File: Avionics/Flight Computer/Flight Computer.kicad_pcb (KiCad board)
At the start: 4 copper layers, 50 x 40 mm, 198 parts, among them J1 ERF8-040-05.0-S-DV-K, J2 ERF8-040-05.0-S-DV-K, J3 473460001, J4 734120110, J5 734120110, J6 734120110, U1 CC1310F128RGZR, U10 Logo, U11 Logo, U12 ATSAME70Q21A-AN, U2 CC1190RGVR, U3 CC2650F128RGZR, U4 CC2592RGVR, U5 MPU-9250, U6 LP5521YQ, U7 LPS25HB, U8 MAX17243, U9 MAX-M8W, Y1 9HT11-32.768KDZB-T, Y2 7V-16.000MAHJ-T, Y3 XRCGB24M000F2P00R0, Y5 XRCGB24M000F2P00R0

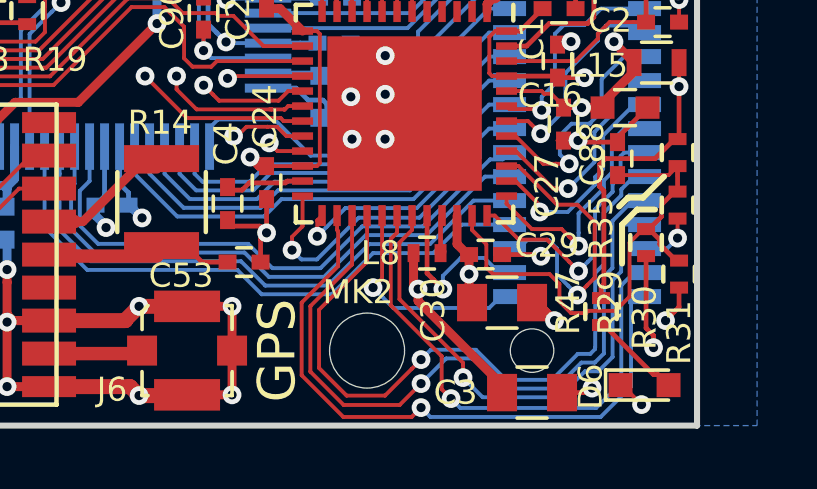
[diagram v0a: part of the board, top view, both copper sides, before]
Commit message: Built outputs and added manufacturing part numbers to make BOM search easier.
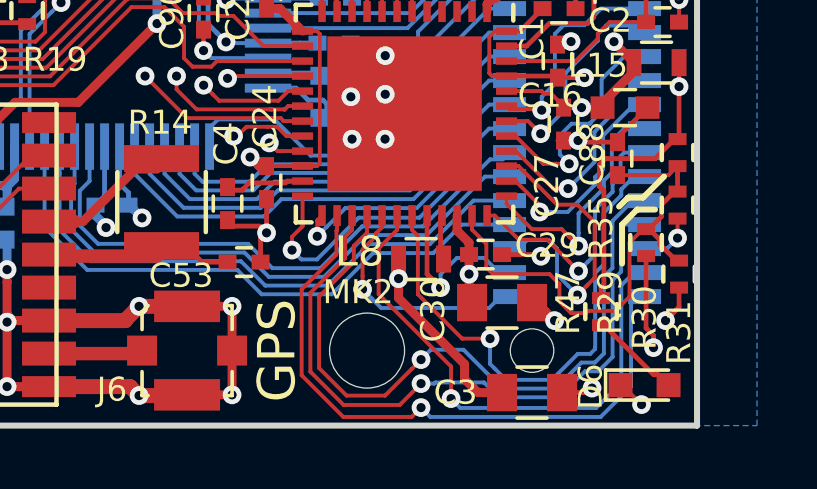
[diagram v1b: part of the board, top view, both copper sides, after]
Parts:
- C1, C2: value 0.1 -> 0.1u
- C10, C8: value 2.2p -> CL05C2R2BB5NNNC
- C12: value 18p -> CL05C2R2BB5NNNC
- C13, C21, C9: value 47p -> GRM1555C1H470FA01D
- C15, C17, C18, C26, C60, C62, C63, C64, C65, C66, C67, C70, C71: value 12p -> GRM1555C1H120GA01D
- C16, C38, C39, C46: value 2.2u -> EMK107BJ225KA-T
- C19, C3, C30, C33, C44, C51, C52: value 22u -> EMK212BBJ226MG-T
- C48, C49: value 10u -> GRM31CR61H106MA12L
- C50: value 2.2u -> UMK212BB7225KG-T
- L1, L14: value 22n -> CIH10T22NJNC
- L13, L3: value 2.2n -> HK10052N2S-T
- L4: value 9.1n -> LQW18AN9N1D00D
- L5: value 4.7n -> HK10054N7S-T
- L6: value 1n -> LQG15HS1N0S02D
- L7: value 2n -> LQG15HS2N0S02D
- L8: value 6.8u -> BRL1608T6R8M; footprint Inductors_SMD:L_0402 -> Inductors_SMD:L_0603
- L9: value 10u -> MLZ1608N100LT000
- R14: value 10 -> ERJ-14YJ100U
- R21: value 22k -> 18k
- U8: value MAX17243 -> MAX17243ETPB
- U9: value MAX-M8W -> MAX-M8W-0
- moved L8 0.28 mm to (90.8, 119.5)
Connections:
- J2 pad 69: /Connectors/900-DIO-18 -> /Connectors/900-DIO-21
- J2 pad 71: /Connectors/900-DIO-17 -> /Connectors/900-DIO-18
- J2 pad 73: /Connectors/900-DIO-21 -> /Connectors/900-DIO-17
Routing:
- net /900MHz Radio/VDDR_CC1310: track 24.6 -> 25.9 mm
- net /Connectors/900-DIO-17: track 23.9 -> 22.6 mm
- net /Connectors/900-DIO-19: track 7.51 -> 8.04 mm

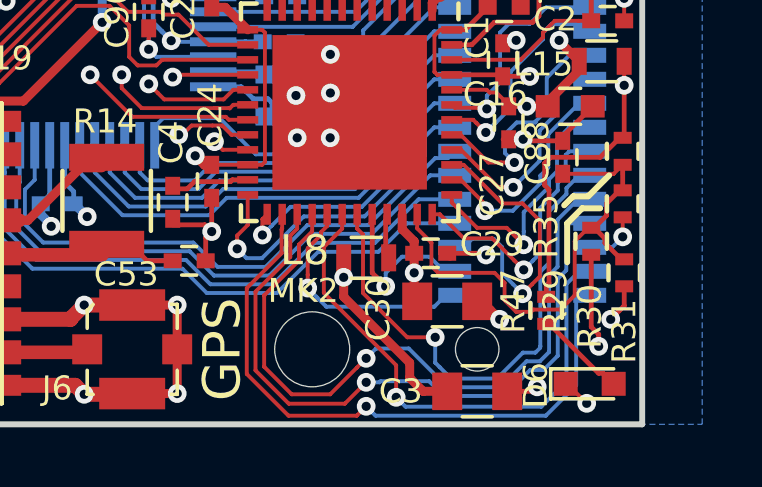
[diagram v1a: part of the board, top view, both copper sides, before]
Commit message: Rebuilt output files and generated a few BOM fixes.
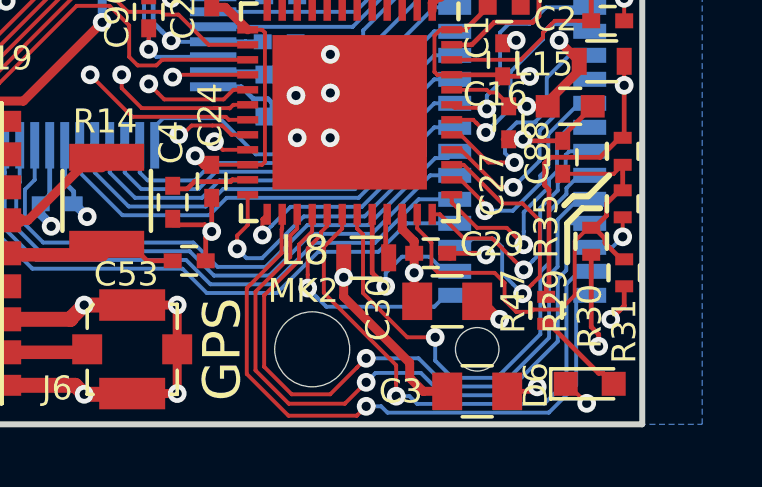
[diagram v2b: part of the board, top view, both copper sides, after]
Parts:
- C11: value 0.2p -> DNP
- C14: value 1p -> CL05C2R2BB5NNNC
- C5: value 3.3p -> GJM1555C1H3R3CB01D
- C6: value 7.5p -> GJM1555C1H7R5CB01D
- C85, C86: value 4.7u -> CC0603KRX5R7BB475
- L12, L18: value 10n -> LQG15HN9N1J02D
- L2: value 7.5n -> LQG15HS7N5J02D
- L4: value LQW18AN9N1D00D -> LQG15HN9N1J02D
- R20: value 5.62k -> 5.6k
- R23: value 2.2 -> ERJ-2GEJ2R2X
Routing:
- net /Connectors/900-DIO-18: track 23.6 -> 23.0 mm

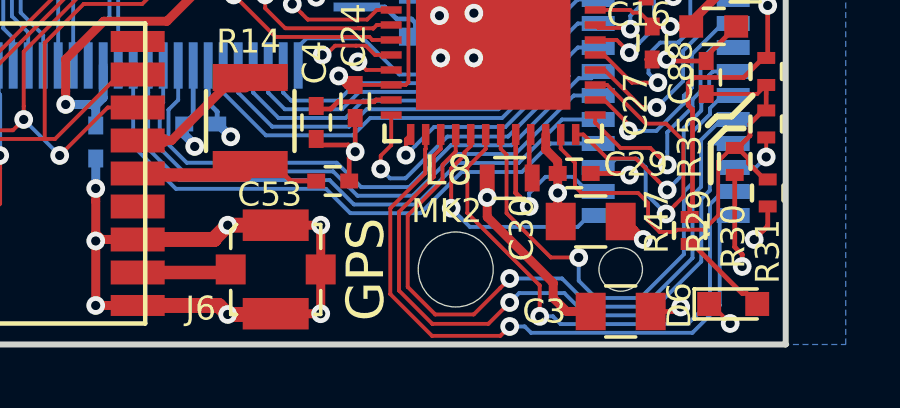
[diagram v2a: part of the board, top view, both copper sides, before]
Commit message: Updated more manufacturing part numbers for macrofab compatibility.
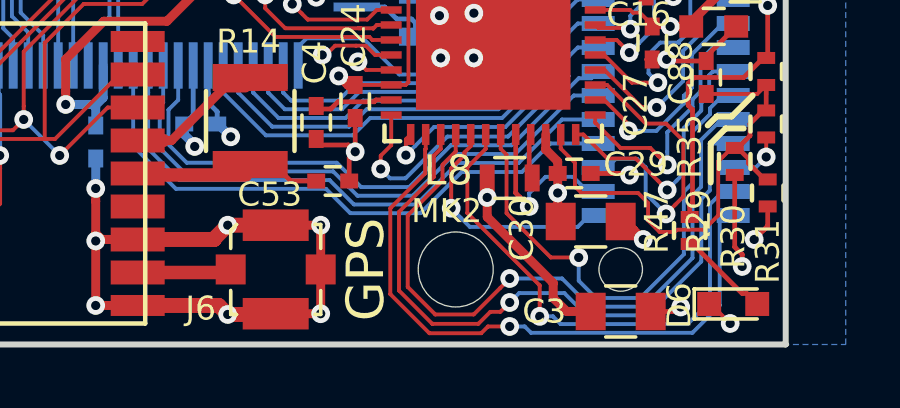
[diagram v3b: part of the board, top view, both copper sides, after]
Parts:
- C92, C93: value 0.47u -> GRM155R61C474KE01D
- D3: value CLX6D-FKB -> CLX6D-FKB-CMPQSGKBB7A363
- D4, D5, D8: value LED-0603-GREEN -> MF-LED-0603-GREEN
- D6: value LED-0603-RED -> MF-LED-0603-RED
- J4, J5, J6: value 734120110 -> 0734120110
- L10, L11, L15: value BLM18HE152SN1 -> BLM18HE152SN1D
- R4: value 3.3k -> RC0402FR-073K3L
- R8: value 3.9k -> RC0402FR-073K9L
- U6: value LP5521YQ -> LP5521YQ/NOPB
- U7: value LPS25HB -> LPS25HBTR
- U8: value MAX17243ETPB -> MAX17243ETPB+

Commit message: Fixed connector part number
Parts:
- J1, J2: value ERF8-040-05.0-S-DV-K -> ERF8-040-05.0-S-DV-K-TR
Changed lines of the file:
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@@
       (effects (font (size 0.8 0.8) (thickness 0.13)) (justify mirror))
     )
-    (fp_text value ERF8-040-05.0-S-DV-K (at 0 0 90) (layer B.Fab)
+    (fp_text value ERF8-040-05.0-S-DV-K-TR (at 0 0 90) (layer B.Fab)
       (effects (font (size 0.9 0.9) (thickness 0.1)) (justify mirror))
     )
@@
       (effects (font (size 0.8 0.8) (thickness 0.13)) (justify mirror))
     )
-    (fp_text value ERF8-040-05.0-S-DV-K (at 0 0 90) (layer B.Fab)
+    (fp_text value ERF8-040-05.0-S-DV-K-TR (at 0 0 90) (layer B.Fab)
       (effects (font (size 0.9 0.9) (thickness 0.1)) (justify mirror))
     )

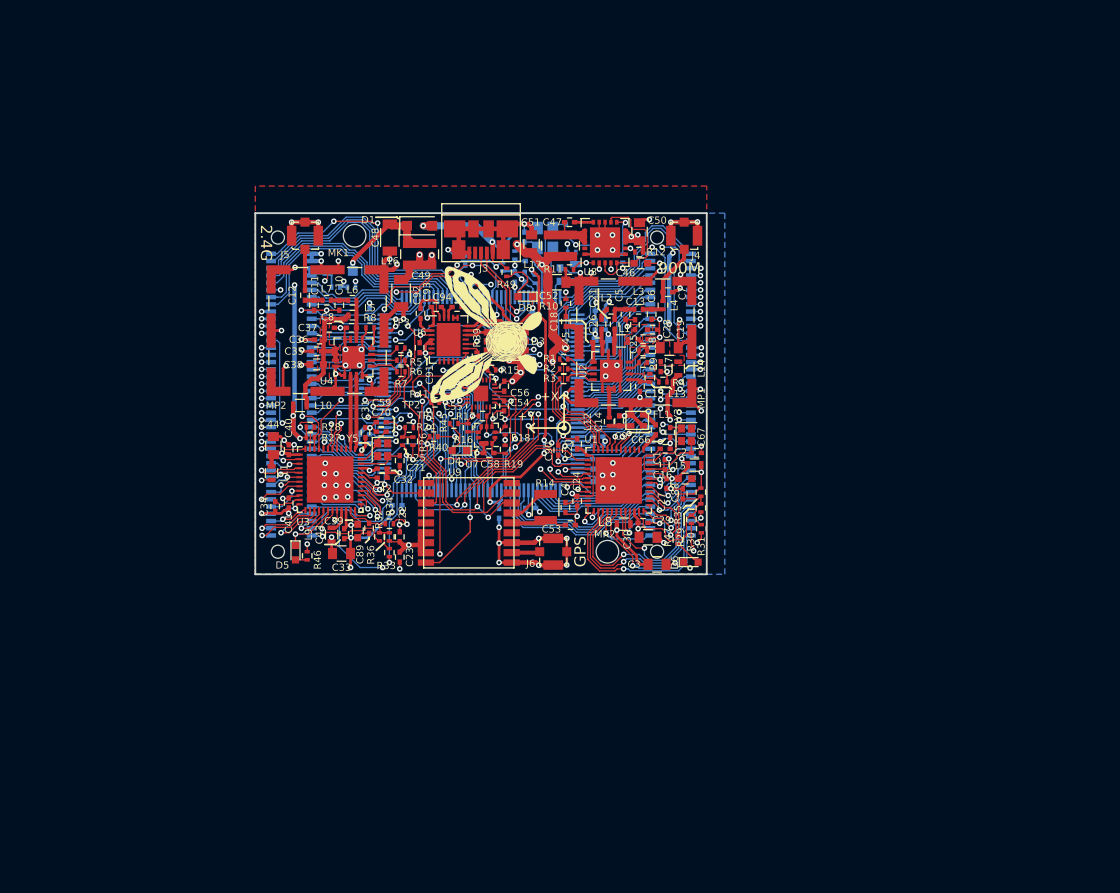
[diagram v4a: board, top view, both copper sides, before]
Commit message: Finished rerouting and power supply update. Replaced connectors and did initial replacement.
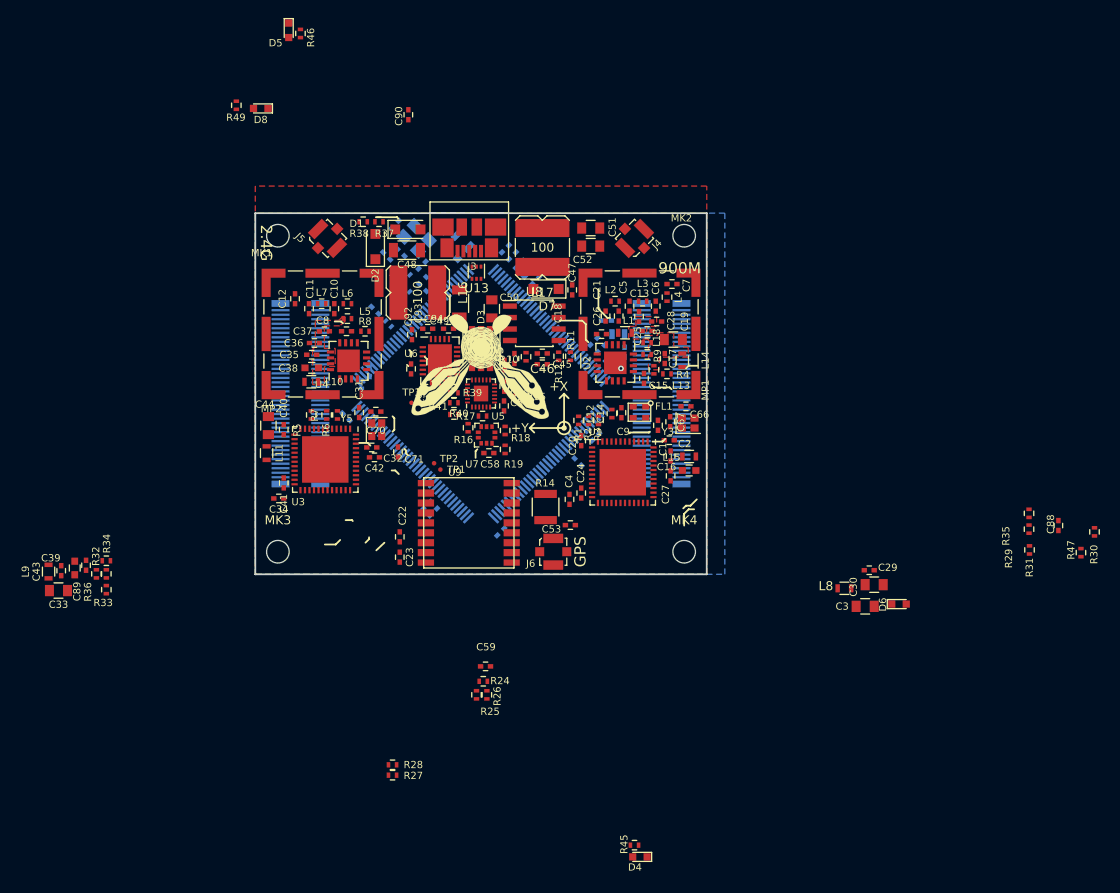
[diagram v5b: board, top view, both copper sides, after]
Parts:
- removed R13: 10k, Resistors_SMD:R_0402
- added C95: GRM1555C1H120GA01D, Capacitors_SMD:C_0402, F.Cu at (78.7, 101.1)
- added D7: SS24FL, Diodes_SMD:D_SOD-123F, F.Cu at (82.2, 93.4)
- added MK3: Mounting_Hole, Mounting_Holes:MountingHole_2.5mm, F.Cu at (52.5, 122.5)
- added MK4: Mounting_Hole, Mounting_Holes:MountingHole_2.5mm, F.Cu at (97.5, 122.5)
- added U13: NUF2042XV6, TO_SOT_Packages_SMD:SOT-563, F.Cu at (74.5, 91.6)
- C45: value 1n -> 0.01u
- C46: value EMK107BJ225KA-T -> GRM1555C1H120GA01D; footprint Capacitors_SMD:C_0603 -> Capacitors_SMD:C_0402
- D1: value NTS245SFT1G -> SS24FL
- D2: value NTS245SFT1G -> SS24FL; moved to F.Cu
- J1, J2: value ERF8-040-05.0-S-DV-K-TR -> AXK5S80047YG; footprint Connectors_Samtec:ERF8-040-05.0-S-DV-K -> Connectors:AXK5S80047YG
- L16, L17: value 74438356022 -> SRN6045-100M; footprint Inductors_SMD:L_Wuerth_MAPI-4020 -> Inductors_SMD:L_BOURNS-SRN6045
- R11: value 15k -> 18k
- R12: value 100k -> ERJ-2RKF5761X
- R37, R38: moved to F.Cu
- U8: value MAX17243ETPB+ -> TPS54232; footprint Housings_DFN_QFN:QFN-20-1EP_5x5mm_Pitch0.65mm -> Housings_SOIC:SOIC-8_3.9x4.9mm_Pitch1.27mm
- moved R46 57.9 mm to (55.0, 65.1)
- moved D5 57.9 mm to (53.7, 64.8)
- moved R45 50.8 mm to (92.0, 155.0)
- moved D4 49.2 mm to (92.6, 156.3)
- moved R30 44.7 mm to (143.0, 120.3)
- moved R47 44.7 mm to (141.4, 122.6)
- moved C88 41.7 mm to (138.9, 119.6)
- moved C90 40.7 mm to (67.0, 74.1)
- moved R28 38.5 mm to (65.2, 146.1)
- moved R27 38.5 mm to (65.2, 147.2)
- moved R31 36.4 mm to (135.8, 122.3)
- moved R29 36.4 mm to (135.7, 120.0)
- moved R35 36.4 mm to (135.7, 118.2)
- moved MK2 36.0 mm to (97.5, 87.5)
- moved D8 36.0 mm to (50.6, 73.4)
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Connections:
- C46 pad 1: /Power/BIAS -> GND
- C46 pad 2: GND -> Net-(C46-Pad2)
- J1 pad 1: GND -> Net-(J1-Pad1)
- J1 pad 10: /Connectors/PA31 -> Net-(J1-Pad10)
- J1 pad 11: /Connectors/PD9 -> Net-(J1-Pad11)
- J1 pad 12: /Connectors/PA29 -> Net-(J1-Pad12)
- J1 pad 13: /Connectors/PC18 -> Net-(J1-Pad13)
- J1 pad 14: /Connectors/PC19 -> Net-(J1-Pad14)
- J1 pad 15: /Connectors/PA28 -> Net-(J1-Pad15)
- J1 pad 16: /Connectors/PA30 -> Net-(J1-Pad16)
- J1 pad 17: /Connectors/PD8 -> Net-(J1-Pad17)
- J1 pad 18: +3V3 -> Net-(J1-Pad18)
- J1 pad 19: /Connectors/PD15 -> Net-(J1-Pad19)
- J1 pad 2: /Connectors/PC21 -> Net-(J1-Pad2)
- J1 pad 20: +3V3 -> Net-(J1-Pad20)
- J1 pad 21: /Connectors/PB4 -> Net-(J1-Pad21)
- J1 pad 22: GND -> Net-(J1-Pad22)
- J1 pad 23: /Connectors/PC17 -> Net-(J1-Pad23)
- J1 pad 24: GND -> Net-(J1-Pad24)
- J1 pad 25: /Connectors/PA0 -> Net-(J1-Pad25)
- J1 pad 26: /Connectors/PB12 -> Net-(J1-Pad26)
- J1 pad 27: /Connectors/PD10 -> Net-(J1-Pad27)
- J1 pad 28: /Connectors/PD25 -> Net-(J1-Pad28)
- J1 pad 29: /Connectors/PC16 -> Net-(J1-Pad29)
- J1 pad 3: GND -> Net-(J1-Pad3)
- J1 pad 30: /Connectors/PD26 -> Net-(J1-Pad30)
- J1 pad 31: /Connectors/PA1 -> Net-(J1-Pad31)
- J1 pad 32: /Connectors/PC6 -> Net-(J1-Pad32)
- J1 pad 33: /Connectors/PD11 -> Net-(J1-Pad33)
- J1 pad 34: /Connectors/PD24 -> Net-(J1-Pad34)
- J1 pad 35: /Connectors/PC14 -> Net-(J1-Pad35)
- J1 pad 36: /Connectors/PA24 -> Net-(J1-Pad36)
- J1 pad 37: /Connectors/PC11 -> Net-(J1-Pad37)
- J1 pad 38: /Connectors/PC5 -> Net-(J1-Pad38)
- J1 pad 39: /CPU-SDA -> Net-(J1-Pad39)
- J1 pad 4: /Connectors/PD6 -> Net-(J1-Pad4)
- J1 pad 40: /Connectors/PA25 -> Net-(J1-Pad40)
- J1 pad 41: /Connectors/PC10 -> Net-(J1-Pad41)
- J1 pad 42: /Connectors/PA26 -> Net-(J1-Pad42)
- J1 pad 43: /Connectors/PB7 -> Net-(J1-Pad43)
- J1 pad 44: /Connectors/PA11 -> Net-(J1-Pad44)
- J1 pad 45: /Connectors/PC9 -> Net-(J1-Pad45)
- J1 pad 46: /Connectors/PA12 -> Net-(J1-Pad46)
- J1 pad 47: /Connectors/PC8 -> Net-(J1-Pad47)
- J1 pad 48: /Connectors/PA27 -> Net-(J1-Pad48)
- J1 pad 49: /Connectors/PD16 -> Net-(J1-Pad49)
- J1 pad 5: +BATT -> Net-(J1-Pad5)
- J1 pad 50: /Connectors/PD28 -> Net-(J1-Pad50)
- J1 pad 51: /CPU-SCK -> Net-(J1-Pad51)
- J1 pad 52: /CPU_RESET_EXT -> Net-(J1-Pad52)
- J1 pad 53: /Connectors/PC28 -> Net-(J1-Pad53)
- J1 pad 54: /Connectors/PB6 -> Net-(J1-Pad54)
- J1 pad 55: /Connectors/PD17 -> Net-(J1-Pad55)
- J1 pad 56: /Connectors/2.4-DIO-7 -> Net-(J1-Pad56)
- J1 pad 57: /Connectors/2.4-ADIO-30 -> Net-(J1-Pad57)
- J1 pad 58: /Connectors/2.4-DIO-8 -> Net-(J1-Pad58)
- J1 pad 59: /Connectors/2.4-ADIO-29 -> Net-(J1-Pad59)
- J1 pad 6: /Connectors/PC20 -> Net-(J1-Pad6)
- J1 pad 60: /Connectors/2.4-DIO-9 -> Net-(J1-Pad60)
- J1 pad 61: /Connectors/2.4-ADIO-28 -> Net-(J1-Pad61)
- J1 pad 62: /Connectors/2.4-DIO-10 -> Net-(J1-Pad62)
- J1 pad 63: /Connectors/2.4-ADIO-27 -> Net-(J1-Pad63)
- J1 pad 64: /Connectors/2.4-DIO-11 -> Net-(J1-Pad64)
- J1 pad 65: /Connectors/2.4-ADIO-26 -> Net-(J1-Pad65)
- J1 pad 66: /Connectors/2.4-DIO-12 -> Net-(J1-Pad66)
- J1 pad 67: /Connectors/2.4-ADIO-25 -> Net-(J1-Pad67)
- J1 pad 68: /Connectors/2.4-DIO-13 -> Net-(J1-Pad68)
- J1 pad 69: /Connectors/2.4-ADIO-24 -> Net-(J1-Pad69)
- J1 pad 7: +BATT -> Net-(J1-Pad7)
- J1 pad 70: /Connectors/2.4-DIO-14 -> Net-(J1-Pad70)
- J1 pad 71: /Connectors/2.4-ADIO-23 -> Net-(J1-Pad71)
- J1 pad 72: /Connectors/2.4-DIO-15 -> Net-(J1-Pad72)
- J1 pad 73: /Connectors/2.4-DIO-18 -> Net-(J1-Pad73)
- J1 pad 74: /2.4-TMSC -> Net-(J1-Pad74)
- J1 pad 75: /Connectors/2.4-DIO-19 -> Net-(J1-Pad75)
- J1 pad 76: /2.4-TCKC -> Net-(J1-Pad76)
- J1 pad 77: /Connectors/2.4-DIO-20 -> Net-(J1-Pad77)
- J1 pad 78: /Connectors/2.4-DIO-16 -> Net-(J1-Pad78)
- J1 pad 79: /2.4_RESET_EXT -> Net-(J1-Pad79)
- J1 pad 8: /Connectors/PD7 -> Net-(J1-Pad8)
- J1 pad 80: /Connectors/2.4-DIO-17 -> Net-(J1-Pad80)
- J1 pad 9: /Connectors/PB5 -> Net-(J1-Pad9)
- J2 pad 1: /Connectors/PB13 -> Net-(J2-Pad1)
- J2 pad 10: /Connectors/PD31 -> Net-(J2-Pad10)
- J2 pad 11: /Connectors/PC25 -> Net-(J2-Pad11)
- J2 pad 12: /Connectors/PE0 -> Net-(J2-Pad12)
- J2 pad 13: /Connectors/PD1 -> Net-(J2-Pad13)
- J2 pad 14: /Connectors/PC27 -> Net-(J2-Pad14)
- J2 pad 15: /Connectors/PD2 -> Net-(J2-Pad15)
- J2 pad 16: /Connectors/PC26 -> Net-(J2-Pad16)
- J2 pad 17: /Connectors/PD3 -> Net-(J2-Pad17)
- J2 pad 18: /Connectors/PC31 -> Net-(J2-Pad18)
- J2 pad 19: /Connectors/PD4 -> Net-(J2-Pad19)
- J2 pad 2: /Connectors/PE3 -> Net-(J2-Pad2)
- J2 pad 20: /Connectors/PC30 -> Net-(J2-Pad20)
- J2 pad 21: /Connectors/PD5 -> Net-(J2-Pad21)
- J2 pad 22: /Connectors/PC29 -> Net-(J2-Pad22)
- J2 pad 23: /Power-Good -> Net-(J2-Pad23)
- J2 pad 24: /Connectors/PC12 -> Net-(J2-Pad24)
- J2 pad 25: /Power-~SHDN~ -> Net-(J2-Pad25)
- J2 pad 26: /Connectors/PC15 -> Net-(J2-Pad26)
- J2 pad 27: +3V3 -> Net-(J2-Pad27)
- J2 pad 28: /Connectors/PC13 -> Net-(J2-Pad28)
- J2 pad 29: +3V3 -> Net-(J2-Pad29)
- J2 pad 3: /Connectors/PC0 -> Net-(J2-Pad3)
- J2 pad 30: /Connectors/PB1 -> Net-(J2-Pad30)
- J2 pad 31: GND -> Net-(J2-Pad31)
- J2 pad 32: /Connectors/PB0 -> Net-(J2-Pad32)
- J2 pad 33: GND -> Net-(J2-Pad33)
- J2 pad 34: /Connectors/PA20 -> Net-(J2-Pad34)
- J2 pad 35: /Connectors/PA14 -> Net-(J2-Pad35)
- J2 pad 36: /Connectors/PA19 -> Net-(J2-Pad36)
- J2 pad 37: /Connectors/PA15 -> Net-(J2-Pad37)
- J2 pad 38: /Connectors/PA18 -> Net-(J2-Pad38)
- J2 pad 39: /Connectors/AUX_SCL -> Net-(J2-Pad39)
- J2 pad 4: /Connectors/PE2 -> Net-(J2-Pad4)
- J2 pad 40: /Connectors/PA17 -> Net-(J2-Pad40)
- J2 pad 41: /Connectors/AUX_SDA -> Net-(J2-Pad41)
- J2 pad 42: /Connectors/PB2 -> Net-(J2-Pad42)
- J2 pad 43: /Connectors/900-DIO-10 -> Net-(J2-Pad43)
- J2 pad 44: /Connectors/PE4 -> Net-(J2-Pad44)
- J2 pad 45: /Connectors/900-DIO-11 -> Net-(J2-Pad45)
- J2 pad 46: /Connectors/PE5 -> Net-(J2-Pad46)
- J2 pad 47: /Connectors/900-DIO-12 -> Net-(J2-Pad47)
- J2 pad 48: /Connectors/PB3 -> Net-(J2-Pad48)
- J2 pad 49: /Connectors/900-DIO-13 -> Net-(J2-Pad49)
- J2 pad 5: /Connectors/PC22 -> Net-(J2-Pad5)
- J2 pad 50: /Connectors/PA21 -> Net-(J2-Pad50)
- J2 pad 51: /Connectors/900-DIO-14 -> Net-(J2-Pad51)
- J2 pad 52: /Connectors/PA22 -> Net-(J2-Pad52)
- J2 pad 53: /Connectors/900-DIO-15 -> Net-(J2-Pad53)
- J2 pad 54: /Connectors/PC1 -> Net-(J2-Pad54)
- J2 pad 55: /Connectors/900-ADIO-30 -> Net-(J2-Pad55)
- J2 pad 56: /Connectors/PC2 -> Net-(J2-Pad56)
- J2 pad 57: /Connectors/900-ADIO-29 -> Net-(J2-Pad57)
- J2 pad 58: /Connectors/PC3 -> Net-(J2-Pad58)
- J2 pad 59: /Connectors/900-ADIO-28 -> Net-(J2-Pad59)
- J2 pad 6: /Connectors/PE1 -> Net-(J2-Pad6)
- J2 pad 60: /Connectors/PC4 -> Net-(J2-Pad60)
- J2 pad 61: /Connectors/900-ADIO-27 -> Net-(J2-Pad61)
- J2 pad 62: /Connectors/PA13 -> Net-(J2-Pad62)
- J2 pad 63: /Connectors/900-ADIO-25 -> Net-(J2-Pad63)
- J2 pad 64: /900-TCKC -> Net-(J2-Pad64)
- J2 pad 65: /Connectors/900-ADIO-24 -> Net-(J2-Pad65)
- J2 pad 66: /900-TMSC -> Net-(J2-Pad66)
- J2 pad 67: /Connectors/900-ADIO-23 -> Net-(J2-Pad67)
- J2 pad 68: /Connectors/PA16 -> Net-(J2-Pad68)
- J2 pad 69: /Connectors/900-DIO-21 -> Net-(J2-Pad69)
- J2 pad 7: /Connectors/PC23 -> Net-(J2-Pad7)
- J2 pad 70: /Connectors/PA23 -> Net-(J2-Pad70)
- J2 pad 71: /Connectors/900-DIO-18 -> Net-(J2-Pad71)
- J2 pad 72: /Connectors/PD27 -> Net-(J2-Pad72)
- J2 pad 73: /Connectors/900-DIO-17 -> Net-(J2-Pad73)
- J2 pad 74: /Connectors/PC7 -> Net-(J2-Pad74)
- J2 pad 75: /900_RESET_EXT -> Net-(J2-Pad75)
- J2 pad 76: /Connectors/900-ADIO-26 -> Net-(J2-Pad76)
- J2 pad 77: /Connectors/900-DIO-20 -> Net-(J2-Pad77)
- J2 pad 78: /Connectors/900-DIO-22 -> Net-(J2-Pad78)
- J2 pad 79: /Connectors/900-DIO-16 -> Net-(J2-Pad79)
- J2 pad 8: /Connectors/PD0 -> Net-(J2-Pad8)
- J2 pad 80: /Connectors/900-DIO-19 -> Net-(J2-Pad80)
- J2 pad 9: /Connectors/PC24 -> Net-(J2-Pad9)
- J3 pad 2: /Connectors/USBD_N -> Net-(J3-Pad2)
- J3 pad 3: /Connectors/USBD_P -> Net-(J3-Pad3)
- R10 pad 1: Net-(R10-Pad1) -> Net-(C46-Pad2)
- R11 pad 1: Net-(R11-Pad1) -> +3V3
- R11 pad 2: GND -> Net-(R11-Pad2)
- R12 pad 1: Net-(C49-Pad1) -> Net-(R11-Pad2)
- R12 pad 2: /Power-~SHDN~ -> GND
- U8 pad 1: Net-(R11-Pad1) -> Net-(C47-Pad2)
- U8 pad 2: +3V3 -> Net-(C49-Pad1)
- U8 pad 3: /Power/BIAS -> /Power-~SHDN~
- U8 pad 4: Net-(R10-Pad1) -> Net-(C95-Pad2)
- U8 pad 5: /Power/BIAS -> Net-(R11-Pad2)
- U8 pad 6: GND -> Net-(C46-Pad2)
- U8 pad 7: /Power-~SHDN~ -> GND
- U8 pad 8: Net-(C49-Pad1) -> Net-(C47-Pad1)
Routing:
- net GND: track 321.7 -> 2.33 mm, vias 118 -> 1
- net +3V3: track 140.8 -> 0.07 mm, vias 32 -> 0
- net Net-(C57-Pad1): track 101.7 -> 0.00 mm, vias 10 -> 0
- net /CPU-SCK: track 72.3 -> 0.00 mm, vias 3 -> 0
- net /CPU-SDA: track 69.6 -> 0.00 mm, vias 4 -> 0
- net /900_RESET_CPU: track 55.1 -> 0.00 mm, vias 3 -> 0
- net /900_RESET_2.4: track 51.5 -> 0.00 mm, vias 3 -> 0
- net /2.4_RESET_900: track 51.3 -> 0.00 mm, vias 2 -> 0
- net /900MHz Radio/VDDS_CC1310: track 47.9 -> 0.00 mm, vias 5 -> 0
- net /GNC_Processor/VBATT: track 45.6 -> 0.00 mm, vias 3 -> 0
- net /Connectors/PD25: track 39.4 -> 0.00 mm, vias 2 -> 0
- net /Connectors/PD26: track 39.0 -> 0.00 mm, vias 2 -> 0
- net /Connectors/PC6: track 37.9 -> 0.00 mm, vias 2 -> 0
- net /Connectors/PD24: track 37.4 -> 0.00 mm, vias 2 -> 0
- net /Connectors/PA25: track 37.0 -> 0.00 mm, vias 2 -> 0
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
